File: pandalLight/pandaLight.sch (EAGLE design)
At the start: 129 parts, among them J1 PJ-037A, U10 TPD12S016PWR, U11 PAN1322, U12 TPS542941PWP, U2 6SLX9TQG144, U3 93LC46BT-I/OT, U4 FT2232HL, U5 TPD12S016PWR, U6 20Mhz, U7 TXB0104PWR, U8 TPD12S016PWR, U9 M25P40-VMN, X1 USBUB-S, X2 HDMI_RECEPTICAL_A, X3 HDMI_RECEPTICAL_A, X4 HDMI_RECEPTICAL_A, X5 PMOD-2X6, X6 PMOD-2X6, Y1 403

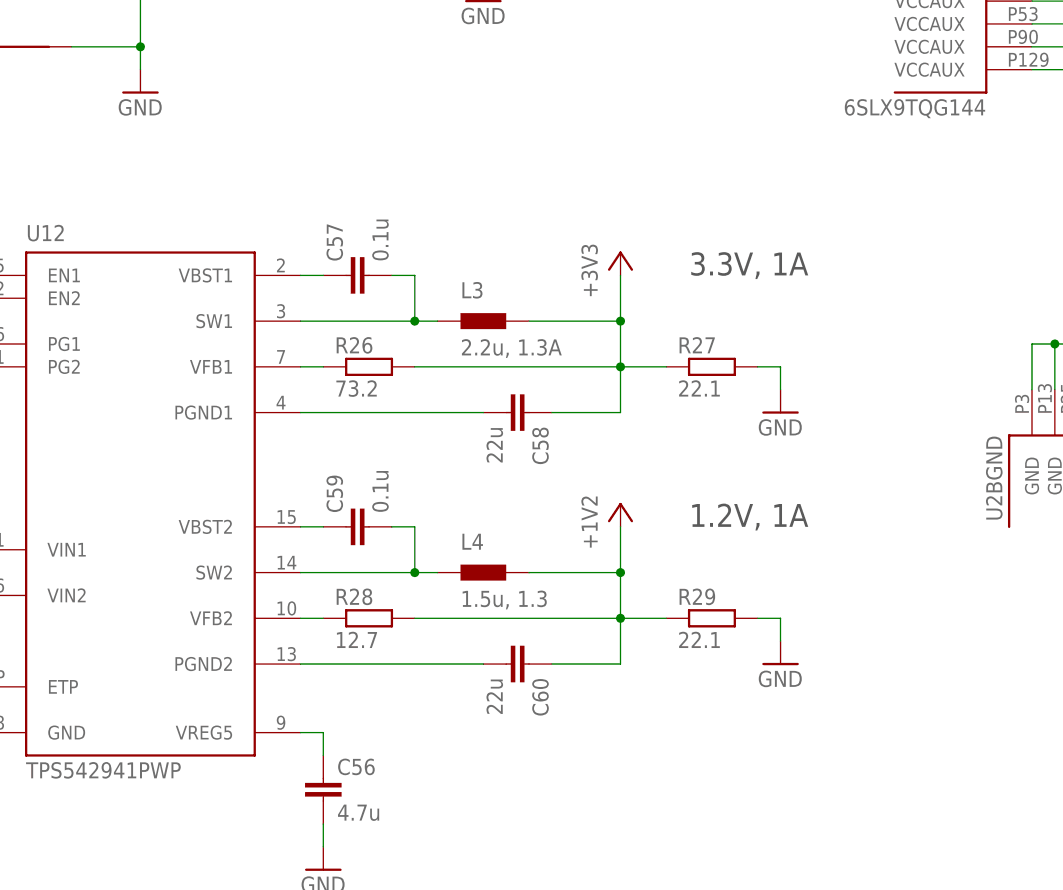
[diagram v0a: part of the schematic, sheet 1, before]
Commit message: Routed new buck regulator
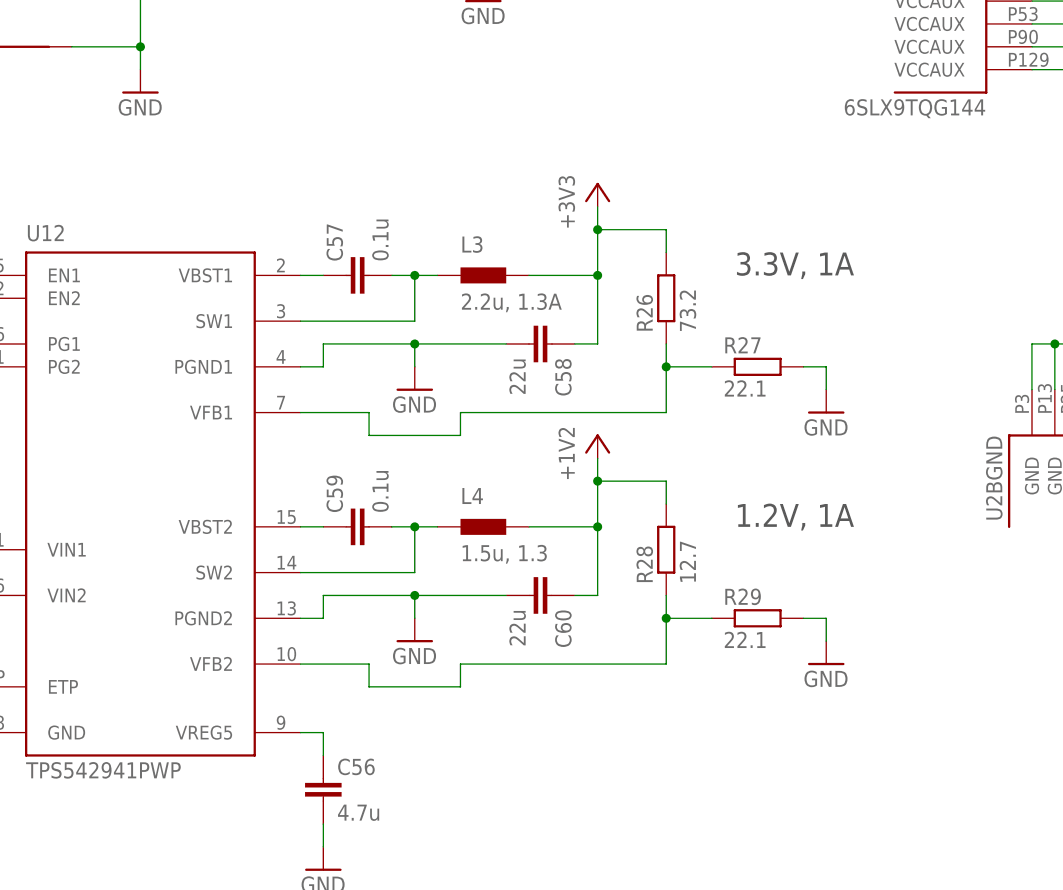
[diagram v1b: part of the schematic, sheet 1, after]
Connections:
- removed net N$17: C58.2, U12.PGND1
- removed net N$20 (its old number): R28.1, U12.VFB2
- removed net N$21: C60.2, U12.PGND2
- new net N$4: R26.1, R27.1, U12.VFB1
- net +1V2: no longer R29.1
- net +3V3: no longer R27.1
- net GND: now also C58.2, C60.2, U12.PGND1, U12.PGND2
- net N$15: now also R28.1, R29.1, U12.VFB2; no longer R26.1, U12.VFB1
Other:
- moved on the sheet: C58, C60, L3, L4, R26, R27, R28, R29

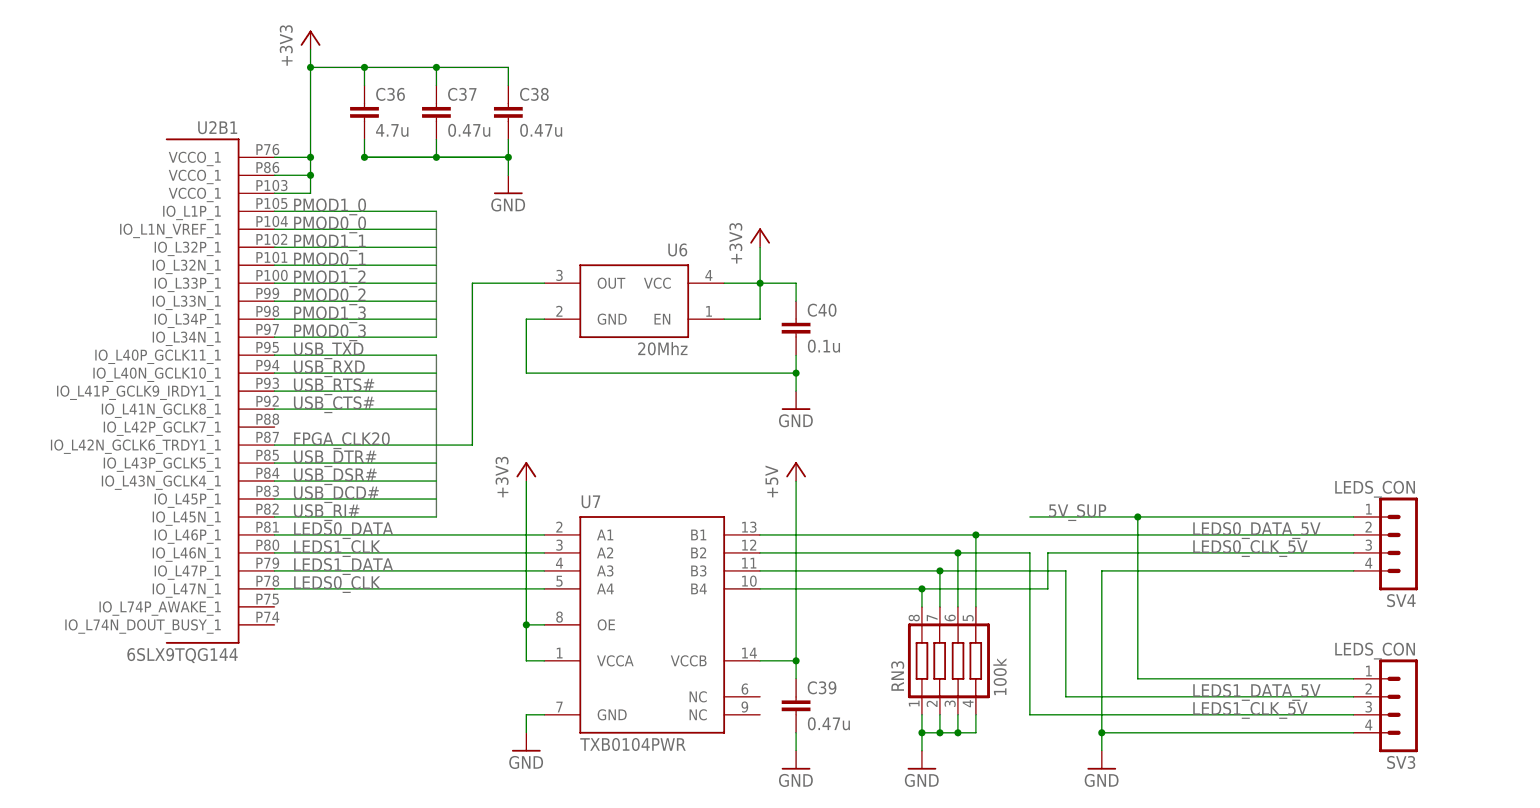
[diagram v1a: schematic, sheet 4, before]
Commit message: Routed everything, corrected unconnected ground pins (due to higher isolation)
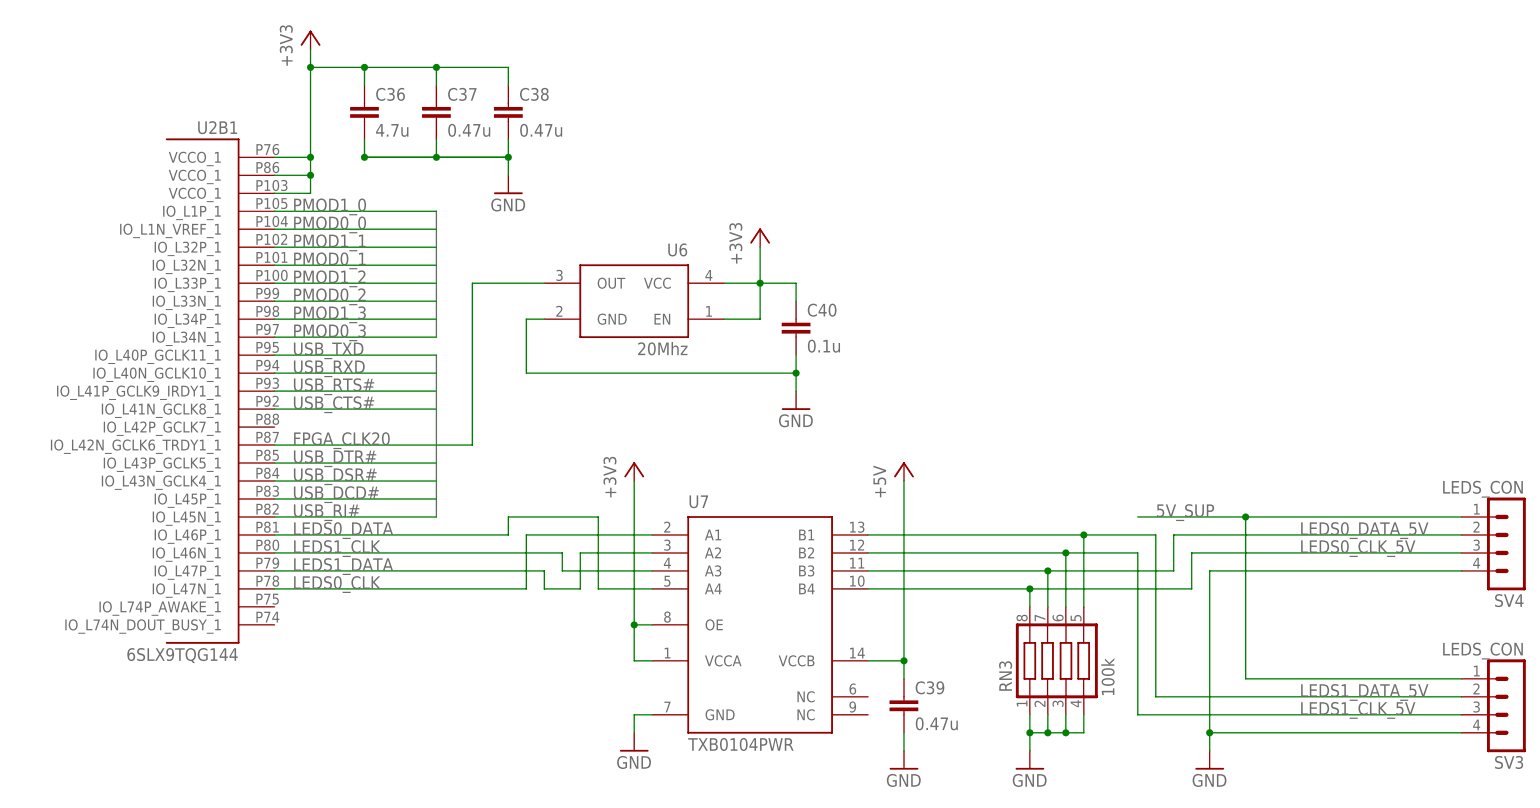
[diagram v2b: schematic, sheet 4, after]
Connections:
- net LEDS0_CLK: now also U7.A1; no longer U7.A4
- net LEDS0_DATA: now also U7.A4; no longer U7.A1
- net LEDS0_DATA_5V: now also RN3.7, U7.B3; no longer RN3.5, U7.B1
- net LEDS1_CLK: now also U7.A3; no longer U7.A2
- net LEDS1_DATA: now also U7.A2; no longer U7.A3
- net LEDS1_DATA_5V: now also RN3.5, U7.B1; no longer RN3.7, U7.B3
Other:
- moved on the sheet: C39, RN3, SV3, SV4, U7

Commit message: Final rev.1 silksreen adjustments; Generated final BOM & partlist; Added Seeedstudio gerber files
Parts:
- U7: PARTNO TXB0104RGYR -> TXB0104PWR
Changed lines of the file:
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@@
 <part name="GND29" library="pandaLight" deviceset="GND" device=""/>
 <part name="U7" library="pandaLight" deviceset="TXB0104" device="PWR" value="TXB0104PWR">
-<attribute name="PARTNO" value="TXB0104RGYR"/>
+<attribute name="PARTNO" value="TXB0104PWR"/>
 </part>
 <part name="RN3" library="pandaLight" deviceset="741C083" device="" value="100k">

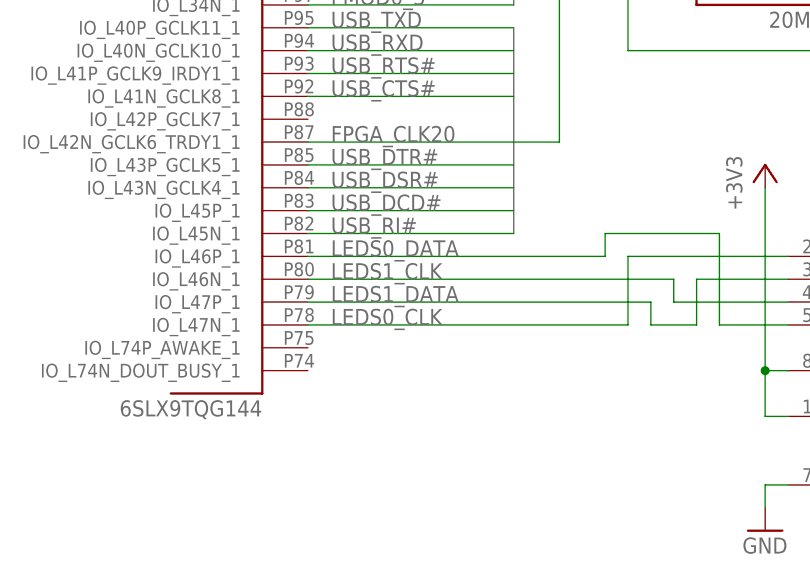
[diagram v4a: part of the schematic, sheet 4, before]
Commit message: Corrected LEDs control wiring error
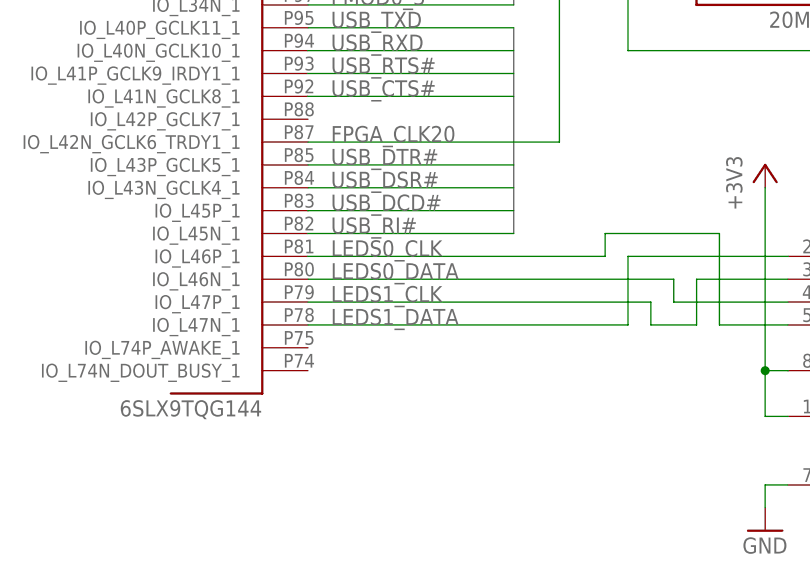
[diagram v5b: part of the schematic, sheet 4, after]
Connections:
- net LEDS0_CLK: now also U2B1.IO_L46P_1, U7.A4; no longer U2B1.IO_L47N_1, U7.A1
- net LEDS0_DATA: now also U2B1.IO_L46N_1, U7.A3; no longer U2B1.IO_L46P_1, U7.A4
- net LEDS1_CLK: now also U2B1.IO_L47P_1, U7.A2; no longer U2B1.IO_L46N_1, U7.A3
- net LEDS1_DATA: now also U2B1.IO_L47N_1, U7.A1; no longer U2B1.IO_L47P_1, U7.A2
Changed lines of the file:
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@@
 </segment>
 </net>
-<net name="LEDS0_CLK" class="0">
+<net name="LEDS1_DATA" class="0">
 <segment>
 <pinref part="U7" gate="G$1" pin="A1"/>
@@
 </segment>
 </net>
-<net name="LEDS1_DATA" class="0">
+<net name="LEDS1_CLK" class="0">
 <segment>
 <pinref part="U7" gate="G$1" pin="A2"/>
@@
 </segment>
 </net>
-<net name="LEDS1_CLK" class="0">
+<net name="LEDS0_DATA" class="0">
 <segment>
 <pinref part="U2" gate="B1" pin="IO_L46N_1"/>
@@
 </segment>
 </net>
-<net name="LEDS0_DATA" class="0">
+<net name="LEDS0_CLK" class="0">
 <segment>
 <pinref part="U7" gate="G$1" pin="A4"/>

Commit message: Replaced PAN1322 with ESP-WROOM-32
Connected it to UART and JTAG; Began routing
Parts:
- removed C52, C53: 0.1u, pandaLight:CAPACITOR0402
- removed R24: 4.7k, pandaLight:RESISTOR0402
- removed R25: 10k, pandaLight:RESISTOR0402
- removed TP1, TP2: TP10SQ, pandaLight:TP10SQ
- added C1: 10u, pandaLight:CAPACITOR0603
- added C2: 0.1u, pandaLight:CAPACITOR0402
- added R1: 10k, pandaLight:RESISTOR0402
- U11: value PAN1322 -> ESP-WROOM-32; device pandaLight:PAN1322 -> pandaLight:ESP-WROOM-32; PARTNO ENW-89841A3KF -> (none)
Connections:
- removed net BT_CTS: U11.P0.7_UARTCTS, U2B3.IO_L52P_3
- removed net BT_RESET#: R24.2, U11.RESET#, U2B3.IO_L83N_VREF_3
- removed net BT_RTS: U11.P0.6_UARTRTS, U2B3.IO_L50N_3
- removed net BT_RX: U11.P0.5_UARTRXD, U2B3.IO_L51N_3
- removed net BT_TX: U11.P0.4_UARTTXD, U2B3.IO_L51P_3
- removed net BT_WAKE: R25.1, U11.P0.14_LPMIN, U2B3.IO_L52N_3
- removed net N$19: TP2.TP, U11.P0.12_SDA0
- removed net N$29: TP1.TP, U11.P0.13_SCL0
- removed net USB_TDO: SV2.4, U2BNA.TDO, U4.ADBUS2
- new net ESP_CTS: U11.SDI/SD1, U2B3.IO_L52P_3
- new net ESP_RTS: U11.SDO/SD0, U2B3.IO_L50N_3
- new net ESP_RX: U11.IO16, U2B3.IO_L51N_3
- new net ESP_TDO: SV2.4, U11.IO15, U4.ADBUS2
- new net ESP_TX: U11.IO17, U2B3.IO_L51P_3
- new net FPGA_TDO: U11.IO12, U2BNA.TDO
- new net N$21: R1.1, U11.EN
- net +3V3: now also C1.1, C2.1, R1.2, U11.3V3; no longer C52.1, C53.1, R25.2, U11.ONOFF, U11.VDD1, U11.VDDUART, U11.VSUPPLY@A4, U11.VSUPPLY@A5, U11.VSUPPLY@A6
- net GND: now also C1.2, C2.2, U11.GND@1, U11.GND@15, U11.GND@38, U11.GND@PAD; no longer C52.2, C53.2, R24.1, U11.VSS@A1, U11.VSS@A11, U11.VSS@A12, U11.VSS@A7, U11.VSS@A9, U11.VSS@C8, U11.VSS@C9, U11.VSS@D7, U11.VSS@D8, U11.VSS@E8, U11.VSS@E9, U11.VSS@F1, U11.VSS@F11, U11.VSS@F12, U11.VSS@F9
- net USB_TCK: now also U11.IO13
- net USB_TMS: now also U11.IO14
